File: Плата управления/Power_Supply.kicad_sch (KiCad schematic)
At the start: 10 parts

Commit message: Поенял усилитель измерительный AD8210 на automotive исполнение INA283AID
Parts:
- D7: footprint (none) -> Package_SO:HTSSOP-20-1EP_4.4x6.5mm_P0.65mm_EP3.4x6.5mm
- L1: footprint (none) -> Inductor_SMD:L_Murata_LQH55DN_5.7x5.0mm
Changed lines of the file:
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@@
       (effects (font (size 1.27 1.27)))
     )
-    (property "Footprint" "" (at 139.7 71.12 0)
+    (property "Footprint" "Package_SO:HTSSOP-20-1EP_4.4x6.5mm_P0.65mm_EP3.4x6.5mm" (at 139.7 71.12 0)
       (effects (font (size 1.27 1.27)) hide)
     )
@@
       (effects (font (size 1.27 1.27)))
     )
-    (property "Footprint" "" (at 139.7 62.23 0)
-      (effects (font (size 1.27 1.27)) hide)
-    )
+    (property "Footprint" "Inductor_SMD:L_Murata_LQH55DN_5.7x5.0mm" (at 139.7 62.23 0)
+      (effects (font (size 1.27 1.27)) hide)
+    )

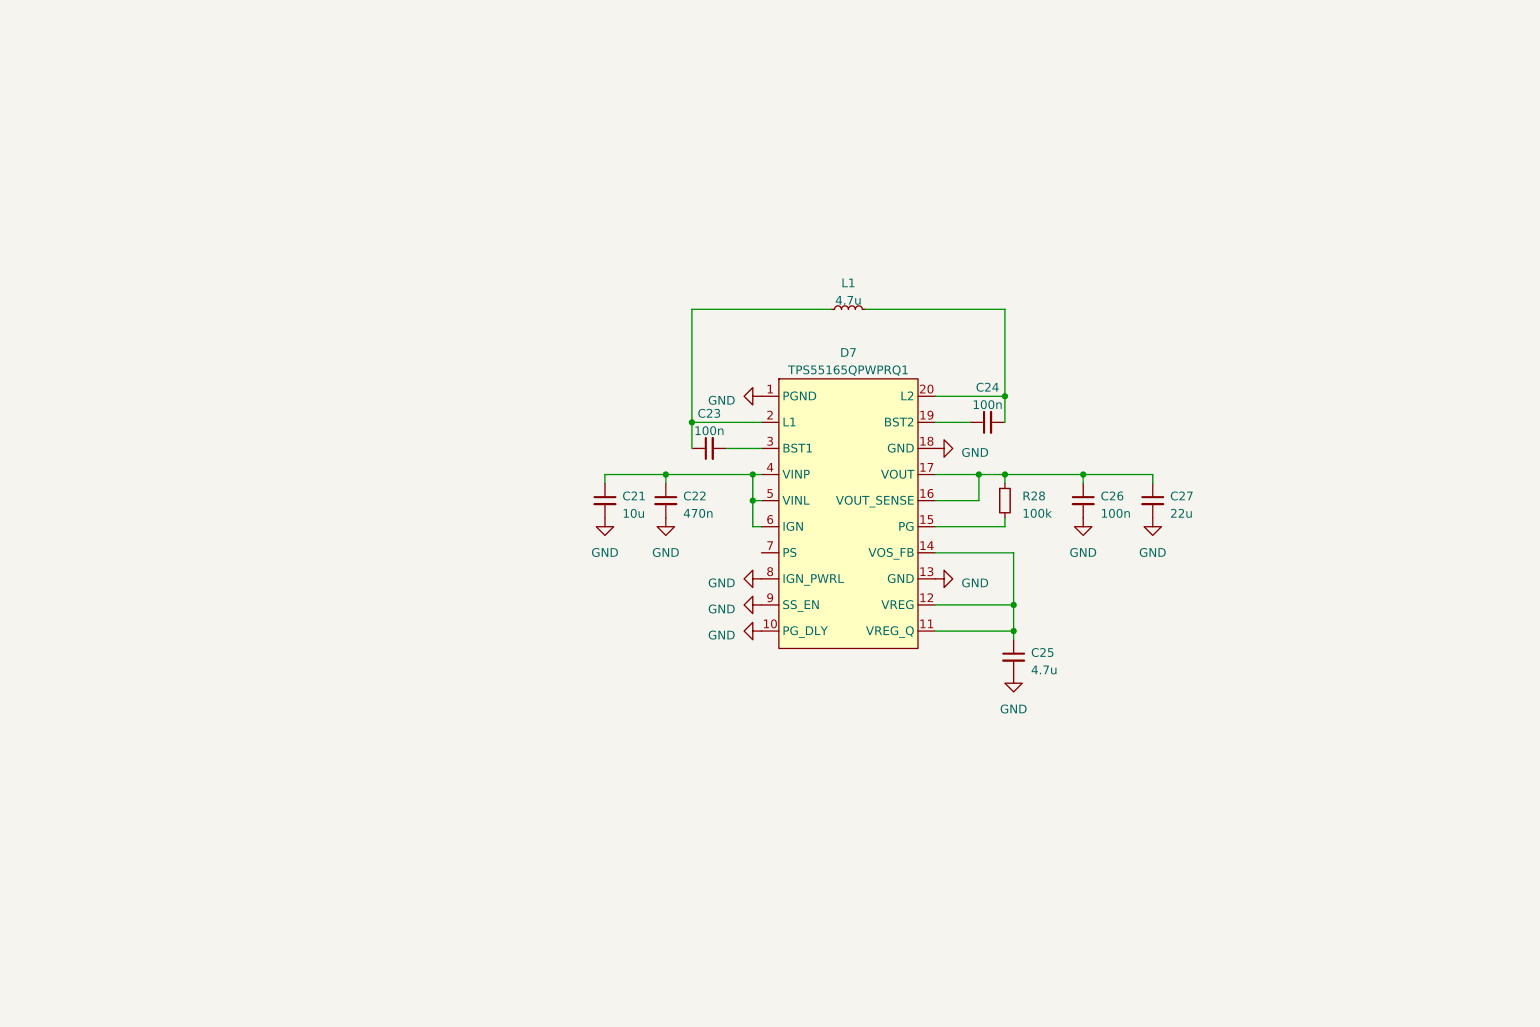
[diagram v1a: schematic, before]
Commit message: Добавил питание 12В в automotive испорлнении и 3.3В
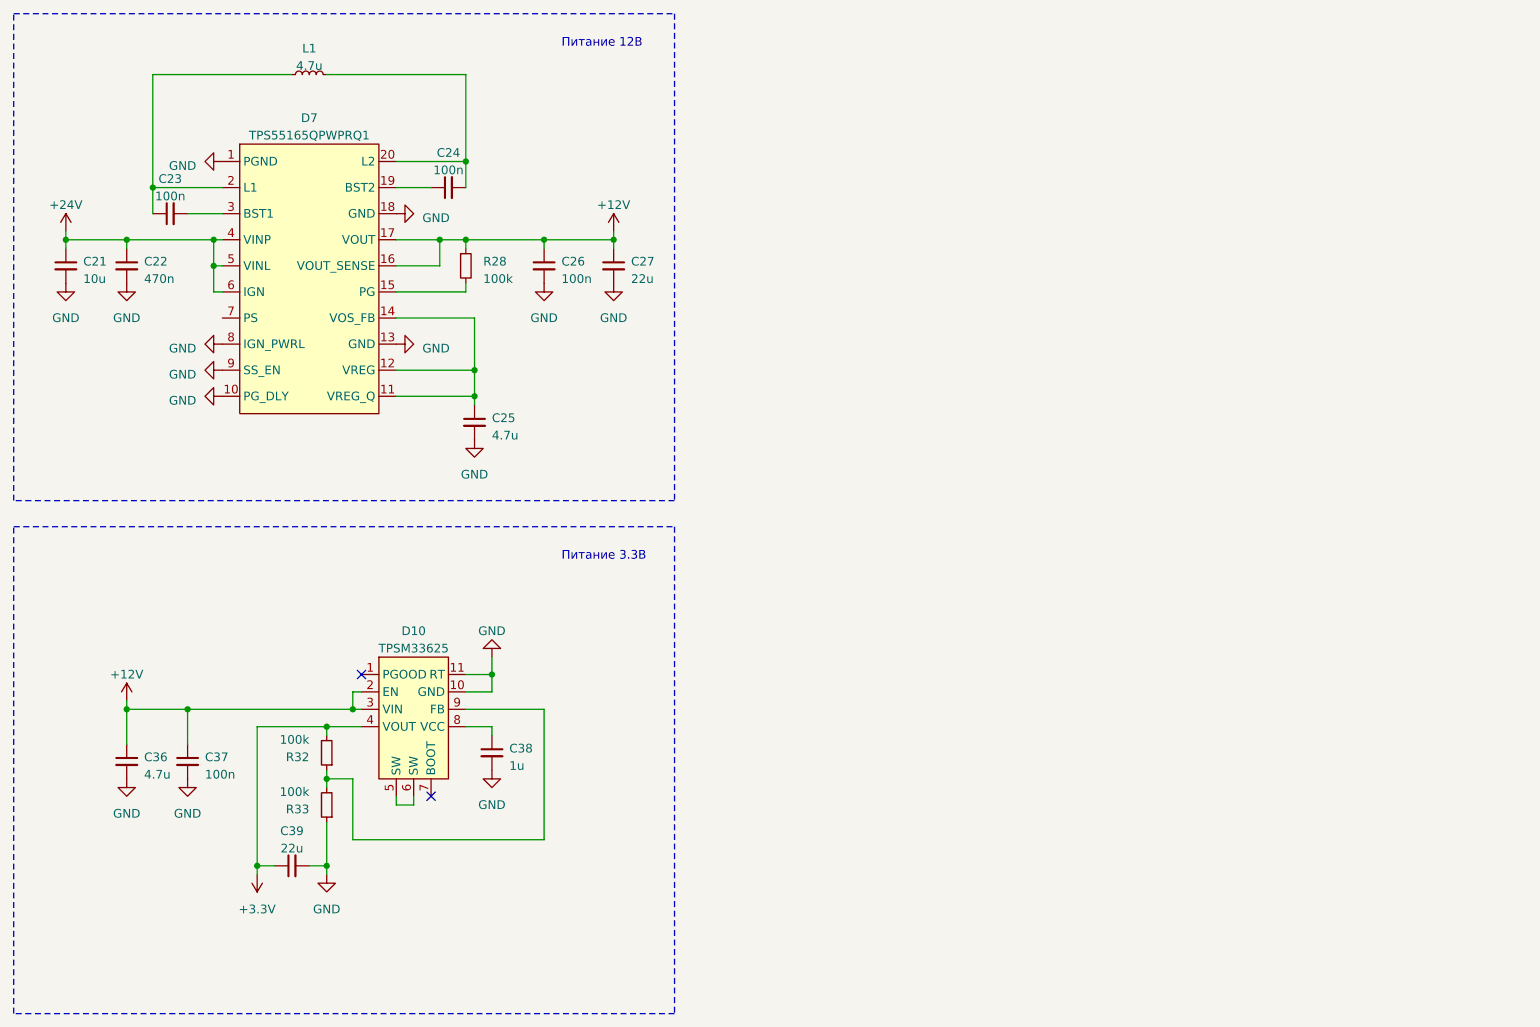
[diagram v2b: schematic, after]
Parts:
- added C36: 4.7u, Capacitor_SMD:C_0805_2012Metric_Pad1.18x1.45mm_HandSolder, symbol Device:C_Small
- added C37: 100n, Capacitor_SMD:C_0603_1608Metric_Pad1.08x0.95mm_HandSolder, symbol Device:C_Small
- added C38: 1u, Capacitor_SMD:C_0603_1608Metric_Pad1.08x0.95mm_HandSolder, symbol Device:C_Small
- added C39: 22u, Capacitor_SMD:C_0805_2012Metric_Pad1.18x1.45mm_HandSolder, symbol Device:C_Small
- added D10: TPSM33625, Convertor_DCDC_My:QFN-FCMOD, symbol Connverter_DCDC_My:TPSM33625
- added R32, R33: 100k, Resistor_SMD:R_0603_1608Metric_Pad0.98x0.95mm_HandSolder, symbol Device:R_Small
- L1: footprint Inductor_SMD:L_Murata_LQH55DN_5.7x5.0mm -> Inductor_my:LQH66SN100M03L
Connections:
- net GND: now also C36.2, C37.2, C38.2, C39.2, D10.10 (GND), D10.11 (RT), R33.1
- net +24V: now reaches C21.1, C22.1, D7.4 (VINP), D7.5 (VINL), D7.6 (IGN)
- net +12V: now reaches C26.1, C27.1, D7.16 (VOUT_SENSE), D7.17 (VOUT), R28.1
- net +12V: now also C36.1, C37.1, D10.2 (EN), D10.3 (VIN)
- new net: D10.9 (FB), R32.1, R33.2
- new net: C38.1, D10.8 (VCC)
- new net: D10.5 (SW), D10.6 (SW)
- new net +3.3V: C39.1, D10.4 (VOUT), R32.2
- no-connect marks 0 -> 2
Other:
- note added: "Питание 12В"
- note added: "Питание 3.3В"
- moved on the sheet: C21, C22, C23, C24, C25, C26, C27, D7, L1, R28

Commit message: Привел в порядок схему
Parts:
- renumbered C21 to C41, C22 to C42, C36 to C43, C23 to C44, C37 to C45, C39 to C46, C24 to C47, C25 to C48, C38 to C49, C26 to C50, C27 to C51, D7 to D8, D10 to D9, L1 to L2, R32 to R29, R33 to R30, R28 to R31

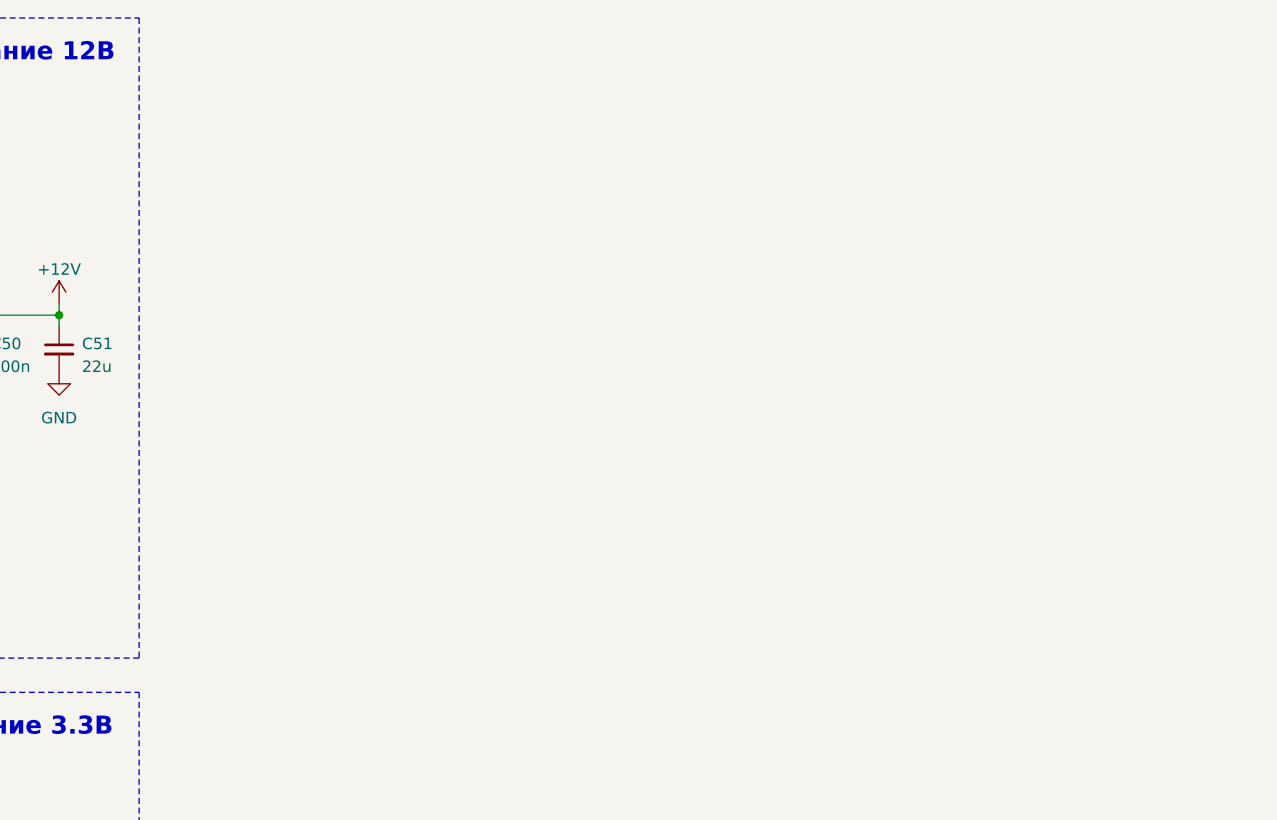
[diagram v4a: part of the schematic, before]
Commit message: Расставил компоненты по плате
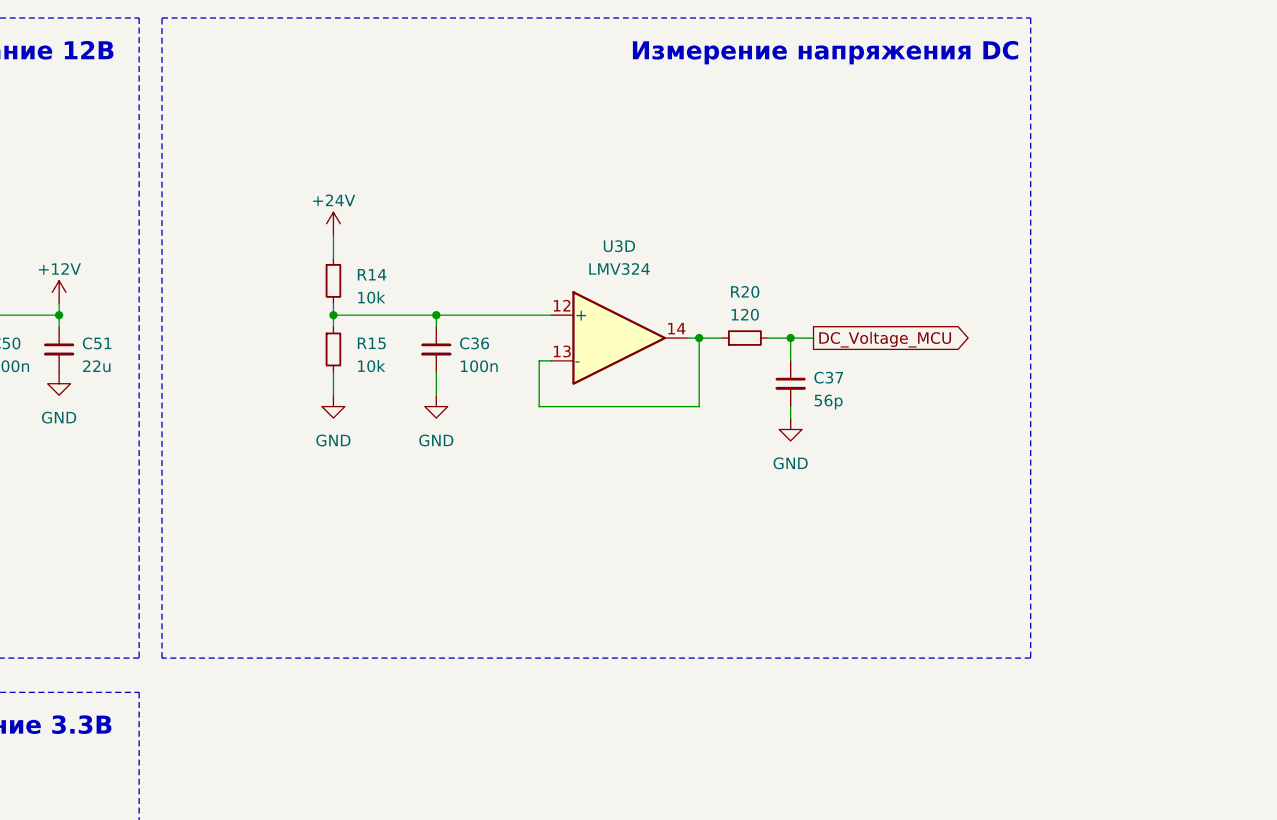
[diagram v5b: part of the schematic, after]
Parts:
- added C36: 100n, Capacitor_SMD:C_0603_1608Metric_Pad1.08x0.95mm_HandSolder, symbol Device:C_Small
- added C37: 56p, Capacitor_SMD:C_0603_1608Metric_Pad1.08x0.95mm_HandSolder, symbol Device:C_Small
- added R14, R15: 10k, Resistor_SMD:R_0603_1608Metric_Pad0.98x0.95mm_HandSolder, symbol Device:R_Small
- added R20: 120, Resistor_SMD:R_0603_1608Metric_Pad0.98x0.95mm_HandSolder, symbol Device:R_Small
- added U3: LMV324, Package_SO:SOIC-14_3.9x8.7mm_P1.27mm, symbol Amplifier_Operational:LMV324
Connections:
- net +24V: now also R14.1
- net GND: now also C36.2, C37.2, R15.2
- new net: C36.1, R14.2, R15.1, U3.12 (+)
- new net: R20.1, U3.13 (-), U3.14
- new net DC_Voltage_MCU: C37.1, R20.2
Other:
- note added: "Измерение напряжения DC"
